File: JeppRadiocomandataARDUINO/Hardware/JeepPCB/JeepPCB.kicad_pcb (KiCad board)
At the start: 2 copper layers, 47.5 x 32.8 mm, 2 parts, among them J1 Conn_01x03_Male

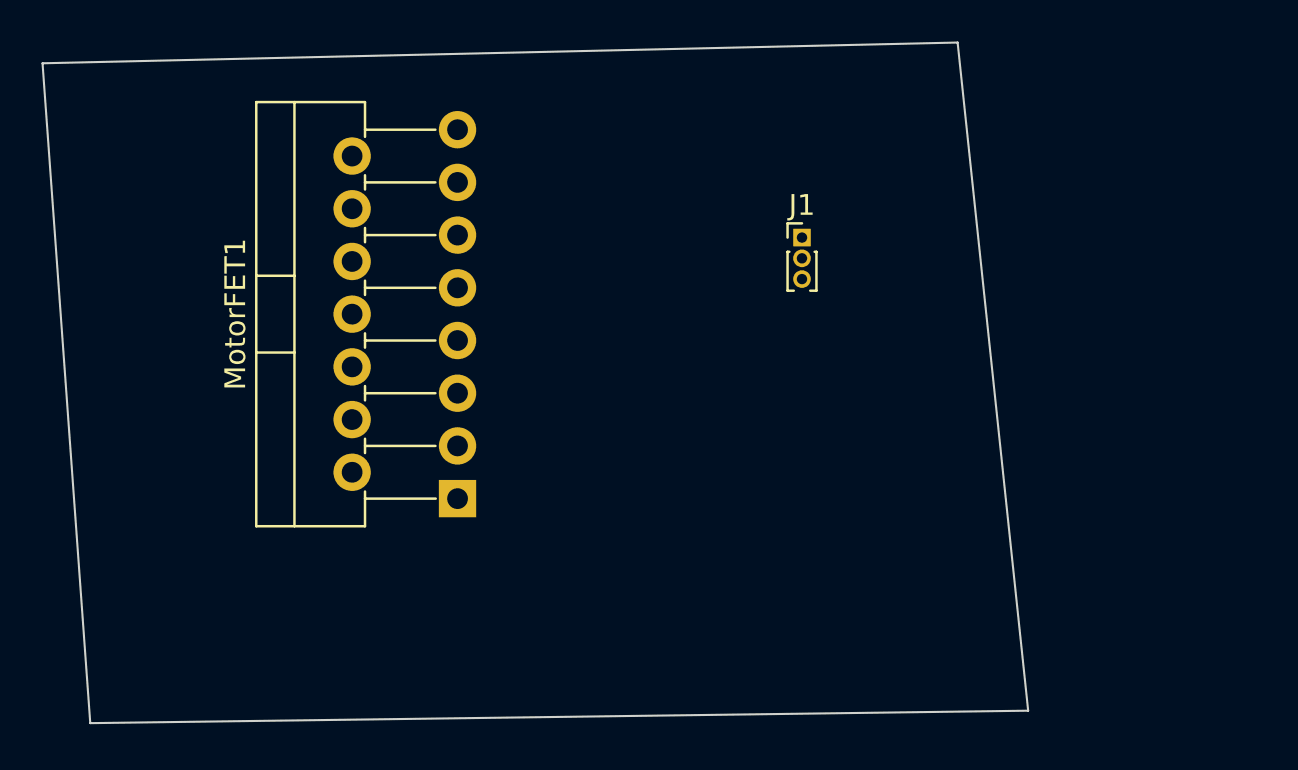
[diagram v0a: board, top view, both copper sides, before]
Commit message: Creazione del PCB personalizzato
Design in KiCad e rimozione delle componenti necessarie
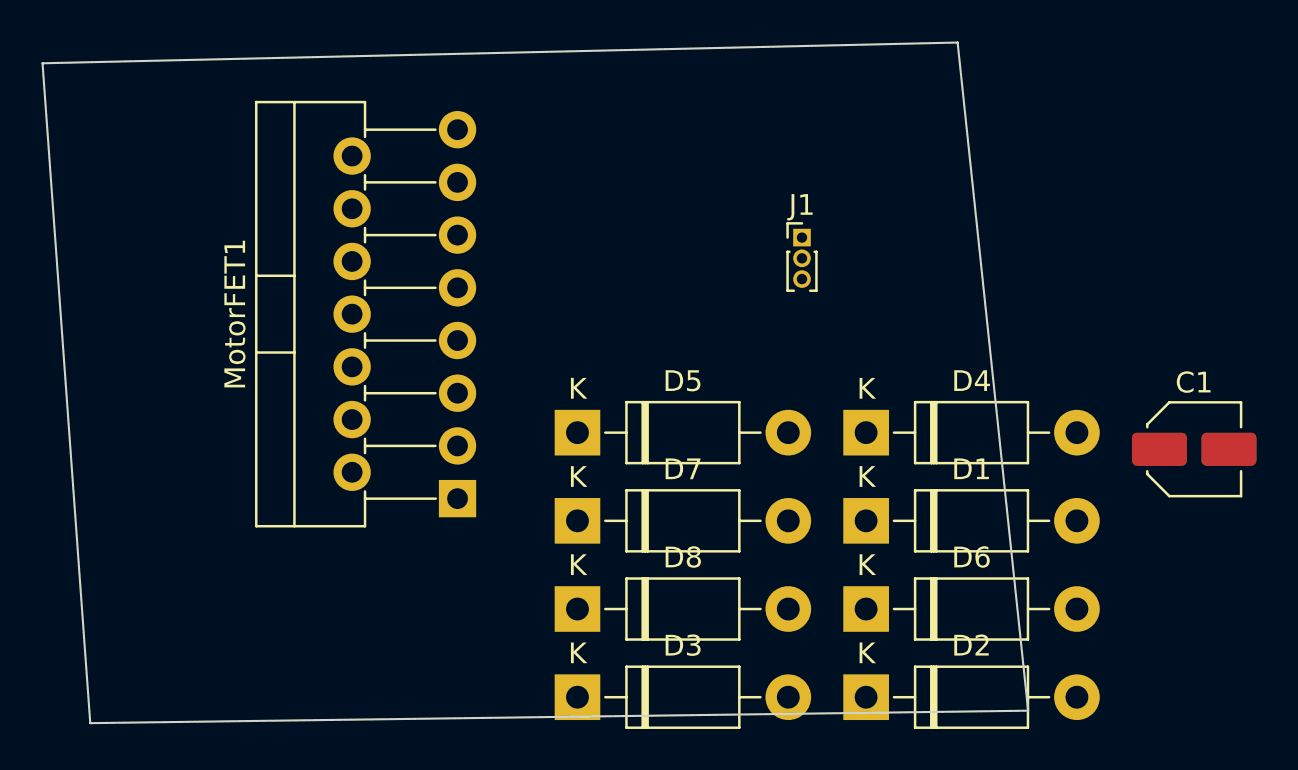
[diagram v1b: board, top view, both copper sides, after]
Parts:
- added C1: 220uF, Capacitor_SMD:C_Elec_4x5.8, F.Cu at (148.7, 73.4)
- added D1: 1N4007, Diode_THT:D_DO-41_SOD81_P10.16mm_Horizontal, F.Cu at (132.9, 76.8)
- added D2: 1N4007, Diode_THT:D_DO-41_SOD81_P10.16mm_Horizontal, F.Cu at (132.9, 85.3)
- added D3: 1N4007, Diode_THT:D_DO-41_SOD81_P10.16mm_Horizontal, F.Cu at (119.0, 85.3)
- added D4: 1N4007, Diode_THT:D_DO-41_SOD81_P10.16mm_Horizontal, F.Cu at (132.9, 72.6)
- added D5: 1N4007, Diode_THT:D_DO-41_SOD81_P10.16mm_Horizontal, F.Cu at (119.0, 72.6)
- added D6: 1N4007, Diode_THT:D_DO-41_SOD81_P10.16mm_Horizontal, F.Cu at (132.9, 81.1)
- added D7: 1N4007, Diode_THT:D_DO-41_SOD81_P10.16mm_Horizontal, F.Cu at (119.0, 76.8)
- added D8: 1N4007, Diode_THT:D_DO-41_SOD81_P10.16mm_Horizontal, F.Cu at (119.0, 81.1)
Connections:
- MotorFET1 pad 1: unconnected-(MotorFET1-Pad1) -> Earth
- MotorFET1 pad 13: Net-(J1-Pad2) -> OUT3
- MotorFET1 pad 14: Net-(J1-Pad1) -> OUT4
- MotorFET1 pad 15: unconnected-(MotorFET1-Pad15) -> Earth
- MotorFET1 pad 2: unconnected-(MotorFET1-Pad2) -> OUT1
- MotorFET1 pad 3: Net-(J1-Pad3) -> OUT2
- MotorFET1 pad 4: unconnected-(MotorFET1-Pad4) -> Net-(MotorFET1-Pad4)
- MotorFET1 pad 8: unconnected-(MotorFET1-Pad8) -> Earth
